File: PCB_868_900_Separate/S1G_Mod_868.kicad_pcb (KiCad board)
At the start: 4 copper layers, 50 x 40 mm, 80 parts, among them J1 S2B-PH-K-S(LF)(SN), J2 20021121-00010C4LF, J3 B4B-PH-K-S(LF)(SN), J5 0475890001-MicroUSBPort, P1 CONN_02X03, Q1 DMG2307L-7, SW1 CUS-12TB, SW2 B3U-1000P, T1 0732511150, T2 0732511150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

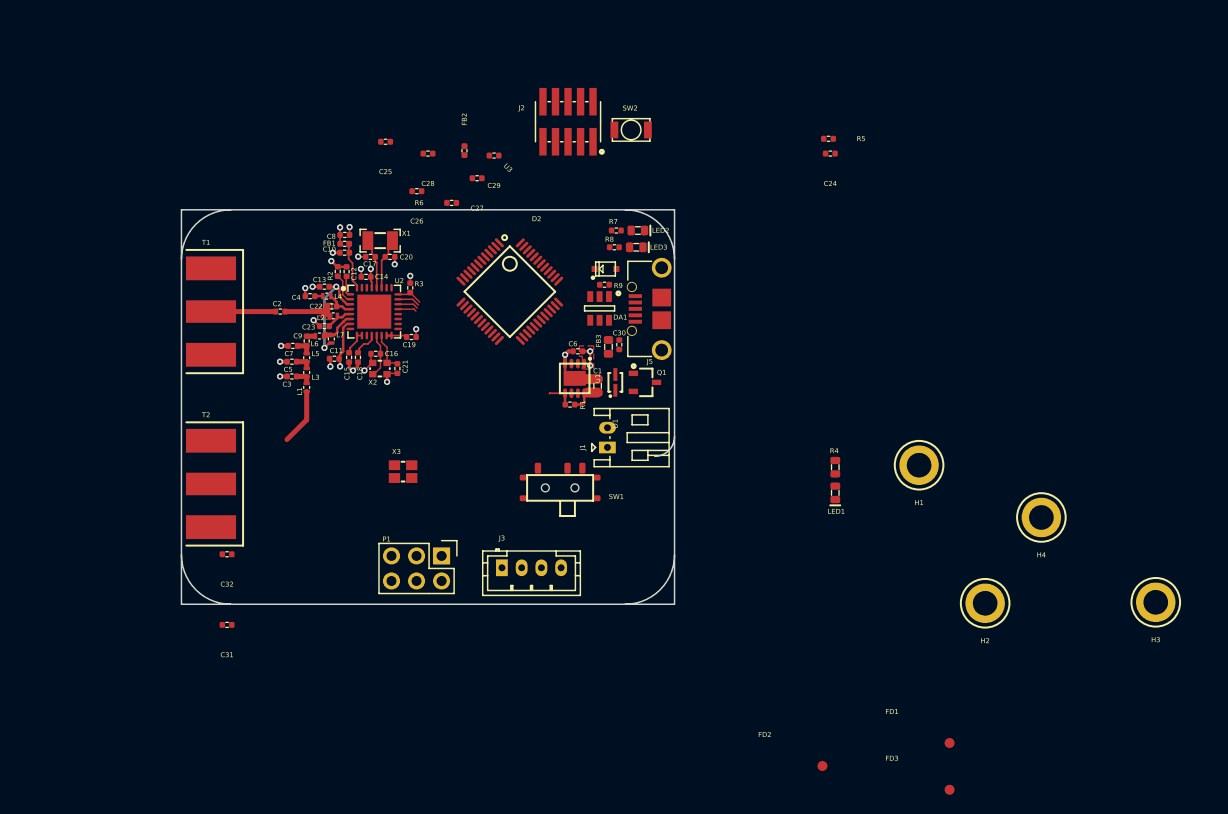
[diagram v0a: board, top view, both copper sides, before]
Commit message: License added and dedicated PA/LNA Match
Working on the separate PA/LNA match version. also added cern license
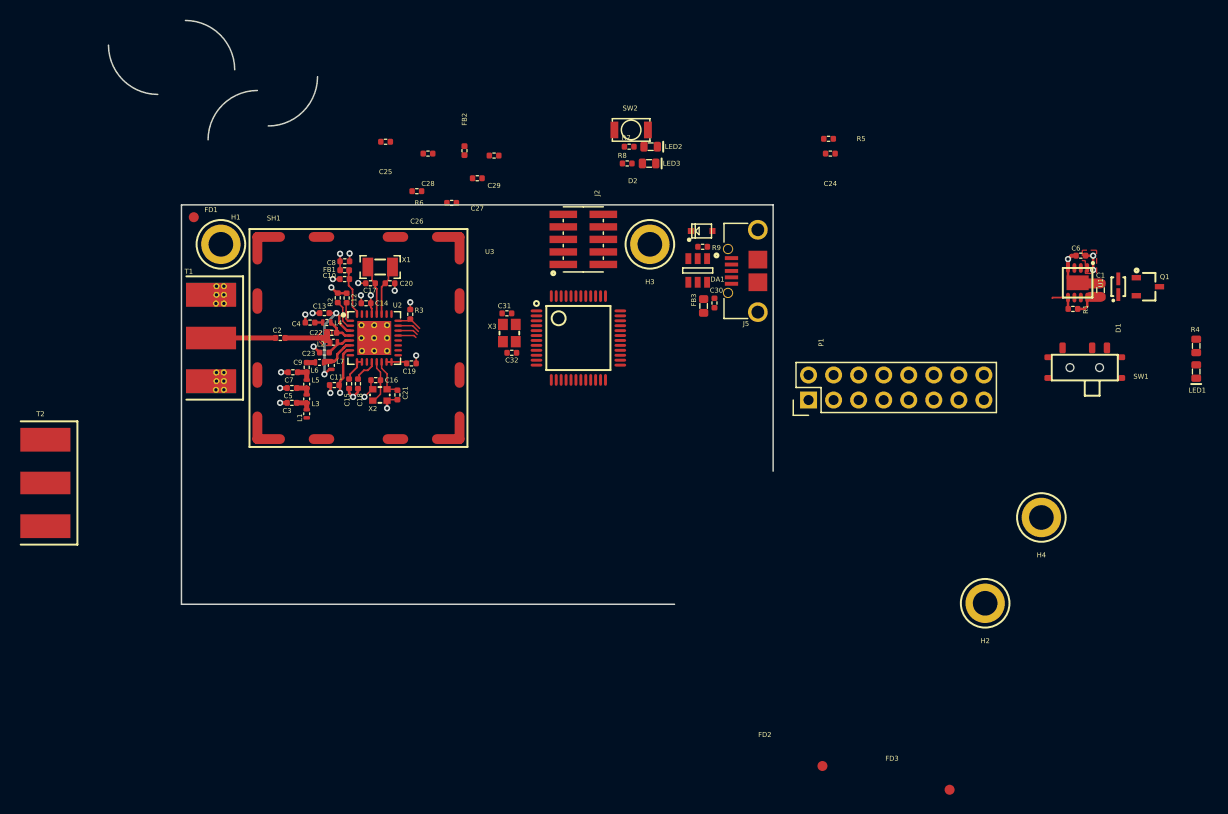
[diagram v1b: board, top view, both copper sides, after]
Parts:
- removed J1: S2B-PH-K-S(LF)(SN), PCB_Footprints:S2B-PH-K-S(LF)(SN)
- removed J3: B4B-PH-K-S(LF)(SN), PCB_Footprints:B4B-PH-K-S(LF)(SN)
- added SH1: 36103205, PCB_Footprints:36103205, F.Cu at (74.5, 48.5)
- P1: value CONN_02X03 -> CONN_02X08; footprint Pin_Headers:Pin_Header_Straight_2x03 -> Pin_Headers:Pin_Header_Straight_2x08
- moved FD1 93.4 mm to (57.8, 36.2)
- moved H1 74.3 mm to (60.5, 39.0)
- moved H3 62.8 mm to (104.0, 39.0)
- moved SW1 54.6 mm to (148.1, 51.5)
- moved D1 51.9 mm to (151.5, 43.3)
- moved Q1 51.9 mm to (154.5, 43.3)
- moved R1 51.9 mm to (146.9, 45.5)
- moved U1 51.9 mm to (147.4, 42.9)
- moved C1 51.9 mm to (149.7, 43.6)
- moved C6 51.9 mm to (147.7, 40.1)
- moved C31 42.5 mm to (89.5, 46.0)
- moved P1 40.4 mm to (120.1, 54.8), turned to 90 degrees
- moved LED1 38.6 mm to (159.4, 51.9)
- moved R4 38.6 mm to (159.4, 49.3)
- moved C32 35.4 mm to (90.0, 50.0), turned to 180 degrees
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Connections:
- P1 pad 1: /MCU - STM32L052K8T6/SPI2_MISO -> Net-(P1-Pad1)
- P1 pad 2: Net-(P1-Pad2) -> /MCU - STM32L052K8T6/SPI2_NSS
- P1 pad 3: /MCU - STM32L052K8T6/SPI2_SCLK -> Net-(P1-Pad3)
- P1 pad 4: /MCU - STM32L052K8T6/SPI2_MOSI -> /MCU - STM32L052K8T6/SPI2_SCLK
- P1 pad 5: /MCU - STM32L052K8T6/SPI2_NSS -> Net-(P1-Pad5)
- P1 pad 6: GND -> /MCU - STM32L052K8T6/SPI2_MISO
- U3 pad 14: /SPI_CS -> /MCU - STM32L052K8T6/SPI2_NSS
- U3 pad 15: /SPI_SCLK -> /MCU - STM32L052K8T6/SPI2_SCLK
- U3 pad 16: /SPI_MISO -> /MCU - STM32L052K8T6/SPI2_MISO
- U3 pad 17: /SPI_MOSI -> /MCU - STM32L052K8T6/SPI2_MOSI
- U3 pad 18: Net-(R8-Pad2) -> Net-(U3-Pad18)
- U3 pad 19: Net-(R7-Pad2) -> Net-(U3-Pad19)
- U3 pad 25: /MCU - STM32L052K8T6/SPI2_NSS -> /SPI_CS
- U3 pad 26: /MCU - STM32L052K8T6/SPI2_SCLK -> /SPI_SCLK
- U3 pad 27: /MCU - STM32L052K8T6/SPI2_MISO -> /SPI_MISO
- U3 pad 28: /MCU - STM32L052K8T6/SPI2_MOSI -> /SPI_MOSI
- U3 pad 42: Net-(U3-Pad42) -> Net-(R8-Pad2)
- U3 pad 43: Net-(U3-Pad43) -> Net-(R7-Pad2)
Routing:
- net Net-(L1-Pad1): track 5.71 -> 0.00 mm
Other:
- board size 50 x 40 mm -> 67.4 x 59.2 mm

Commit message: Progress
Significant progress on the separate PA/LNA matchj implementation.
Formfactor has been devised and is similar to the combined version , so
they go together well. Component placement is mostly complete and board
outline solidified.
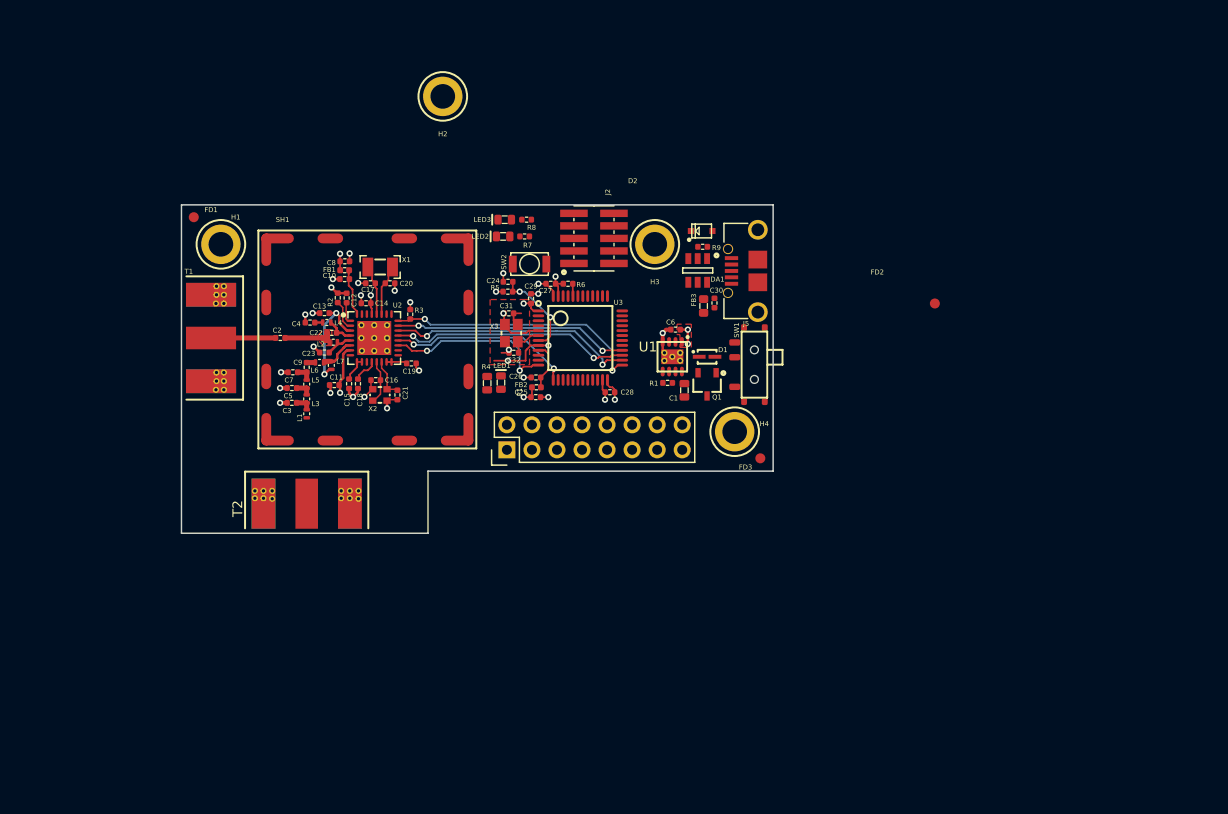
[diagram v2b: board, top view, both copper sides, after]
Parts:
- moved H2 75.3 mm to (83.0, 24.0)
- moved R4 72.0 mm to (87.5, 53.1)
- moved LED1 70.5 mm to (88.9, 53.0), turned to 90 degrees
- moved FD2 48.3 mm to (132.9, 45.0)
- moved Q1 45.8 mm to (109.8, 53.2), turned to 270 degrees
- moved C1 43.4 mm to (107.5, 53.8), turned to 270 degrees
- moved D1 42.3 mm to (109.8, 50.4), turned to 0 degrees
- moved R1 41.8 mm to (105.8, 53.0)
- moved C6 41.8 mm to (106.6, 47.6)
- moved U1 41.8 mm to (106.3, 50.4)
- moved FD3 38.7 mm to (115.2, 60.7)
- moved R5 36.0 mm to (89.6, 43.8), turned to 0 degrees
- moved C24 35.2 mm to (89.6, 42.8), turned to 180 degrees
- moved SW1 33.5 mm to (114.6, 51.2), turned to 90 degrees
- moved H4 32.3 mm to (112.6, 58.0)
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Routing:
- net /SPI_CS: track 2.65 -> 26.4 mm, vias 0 -> 2
- net /SPI_SCLK: track 2.09 -> 25.2 mm, vias 0 -> 2
- net /SPI_MISO: track 1.88 -> 24.4 mm, vias 0 -> 2
- net /SPI_MOSI: track 2.30 -> 23.8 mm, vias 0 -> 2
- net /MCU_IRQ: track 0.00 -> 18.8 mm, vias 0 -> 2
- net /GPIO2: track 0.00 -> 17.6 mm, vias 0 -> 2
- net GND: track 25.0 -> 41.9 mm, vias 18 -> 28
- net +3V3: track 11.5 -> 20.9 mm, vias 6 -> 11
- net /MCU - STM32L052K8T6/NRST: track 0.00 -> 9.20 mm, vias 0 -> 2
- net Net-(C31-Pad1): track 0.00 -> 5.16 mm
- net Net-(C26-Pad1): track 0.00 -> 4.89 mm
- net Net-(C32-Pad1): track 0.00 -> 3.52 mm
- net /VIN: track 3.00 -> 0.00 mm
- net /ON_OFF: track 2.78 -> 0.00 mm
- net Net-(R6-Pad2): track 0.00 -> 1.26 mm
- added copper zone on F.Cu, net GND
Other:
- board size 67.4 x 59.2 mm -> 60 x 33.3 mm

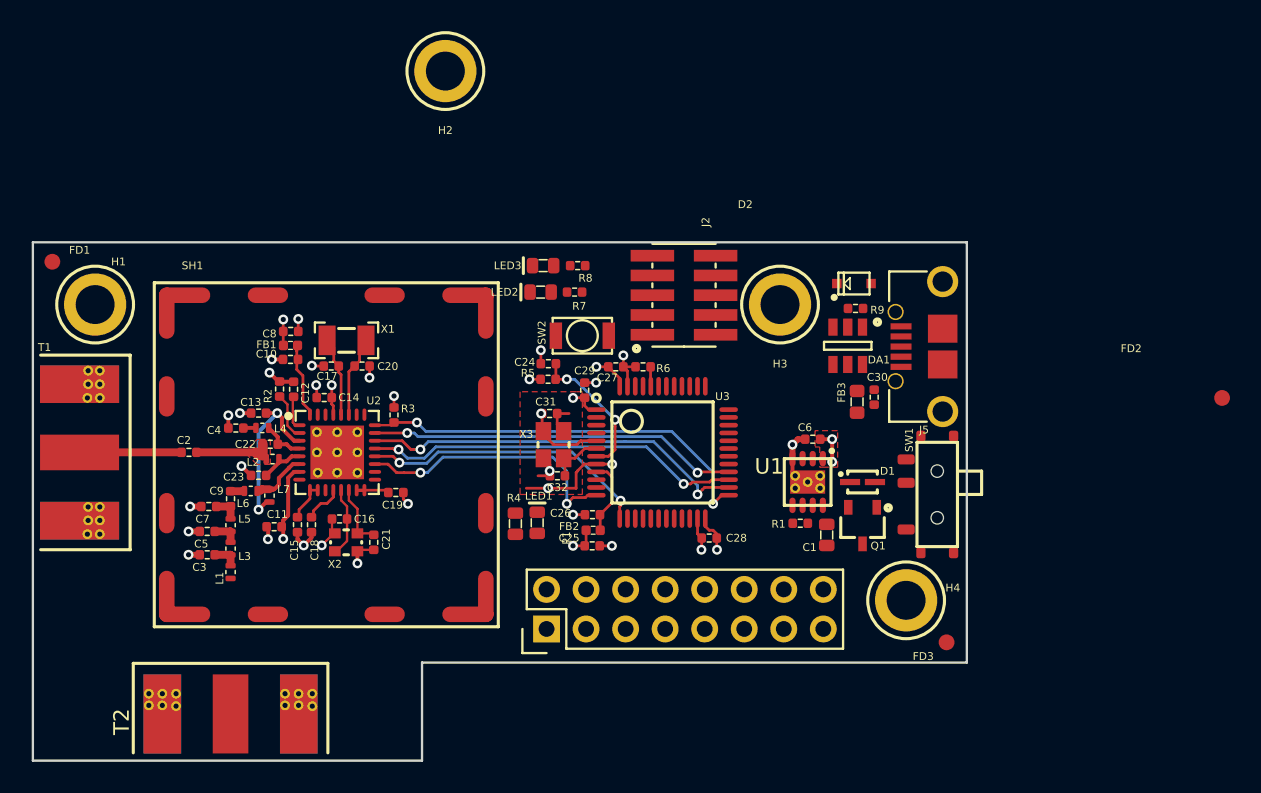
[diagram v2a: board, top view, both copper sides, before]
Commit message: Separate PA/LNA first pass
first pass on PCB complete !
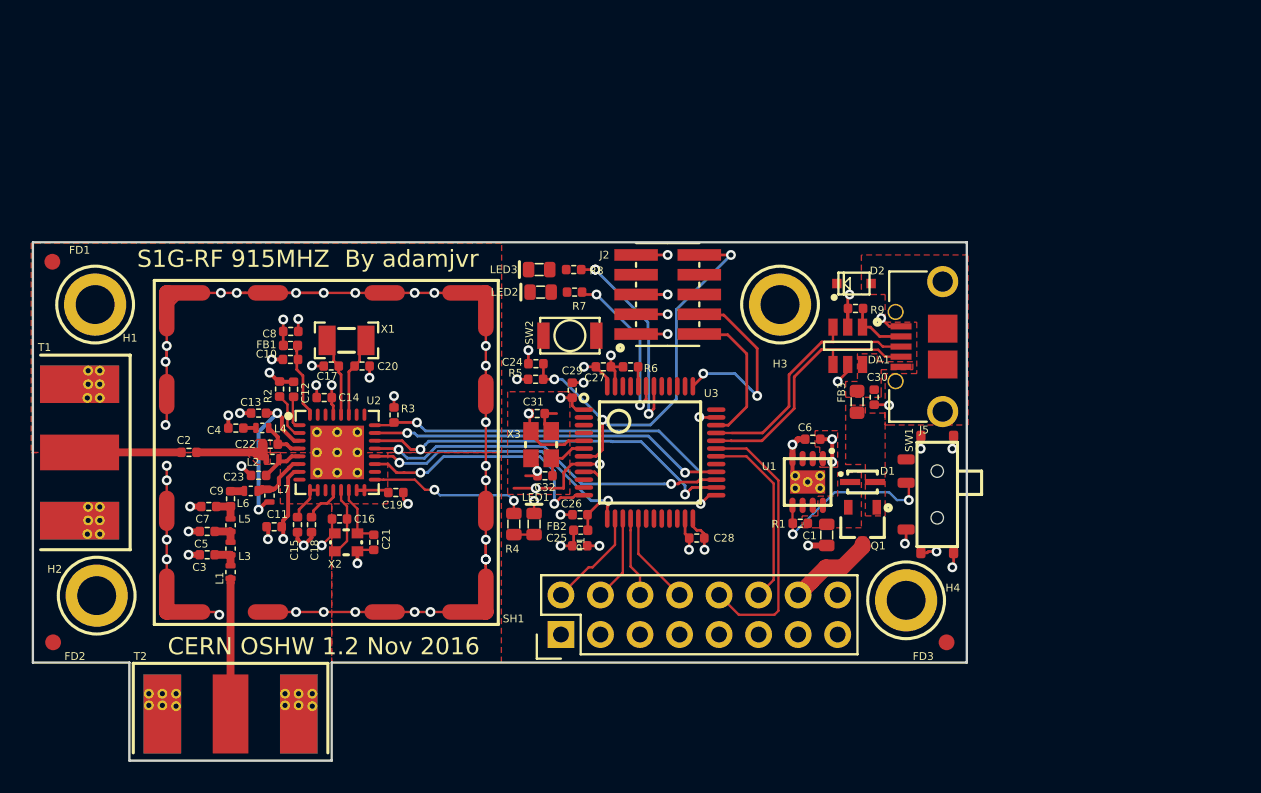
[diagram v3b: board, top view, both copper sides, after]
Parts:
- moved FD2 76.7 mm to (57.8, 60.7)
- moved H2 40.5 mm to (60.6, 57.7)
- moved J2 1.05 mm to (97.3, 38.4)
- moved P1 0.99 mm to (90.4, 60.2)
- moved C24 0.80 mm to (88.8, 42.8)
- moved C25 0.80 mm to (91.6, 54.5)
- moved FB2 0.80 mm to (91.7, 53.5)
- moved C26 0.80 mm to (91.7, 52.5)
- moved C27 0.80 mm to (93.2, 43.0)
- moved C28 0.80 mm to (99.2, 54.0)
- moved C29 0.80 mm to (91.2, 44.5)
- moved C31 0.80 mm to (88.9, 46.0)
- moved C32 0.80 mm to (89.4, 50.0)
- moved R5 0.80 mm to (88.8, 43.8)
- moved R6 0.80 mm to (94.9, 43.0)
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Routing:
- net GND: track 41.9 -> 141.9 mm, vias 28 -> 69
- net /MCU - STM32L052K8T6/NRST: track 9.20 -> 27.5 mm, vias 2 -> 3
- net /MCU - STM32L052K8T6/USART1_RX: track 0.00 -> 17.7 mm
- net /MCU - STM32L052K8T6/USB_DM: track 0.00 -> 16.6 mm
- net /MCU - STM32L052K8T6/USB_DP: track 0.00 -> 16.6 mm
- net Net-(R8-Pad2): track 0.00 -> 13.5 mm, vias 0 -> 3
- net /MCU - STM32L052K8T6/USART1_TX: track 0.00 -> 12.0 mm
- net /ON_OFF: track 0.00 -> 11.8 mm, vias 0 -> 2
- net /MCU - STM32L052K8T6/SWCLK: track 0.00 -> 11.8 mm, vias 0 -> 2
- net Net-(R7-Pad2): track 0.00 -> 10.6 mm, vias 0 -> 2
- net Net-(R4-Pad1): track 0.00 -> 10.3 mm, vias 0 -> 2
- net Net-(L1-Pad1): track 0.00 -> 8.70 mm
- net /MCU - STM32L052K8T6/SWDIO: track 0.00 -> 8.36 mm
- net /MCU - STM32L052K8T6/SPI2_NSS: track 0.00 -> 6.50 mm
- net /MCU - STM32L052K8T6/SPI2_MOSI: track 0.00 -> 6.00 mm
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- added copper zone on F.Cu, net /VBUS
- added copper zone on F.Cu, net /VIN
- added copper zone on F.Cu, net Net-(C30-Pad2)
- added copper zone on F.Cu, net Net-(D2-Pad1)
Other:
- outline, holes or cut-outs redrawn
- board text added: "CERN OSHW 1.2 Nov 2016"
- board text added: "S1G-RF 915MHZ By adamjvr"
